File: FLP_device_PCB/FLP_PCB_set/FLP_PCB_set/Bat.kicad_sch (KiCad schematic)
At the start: 6 parts, among them J7 B2B-PH-K-S, U11 MCP73831-2-OT

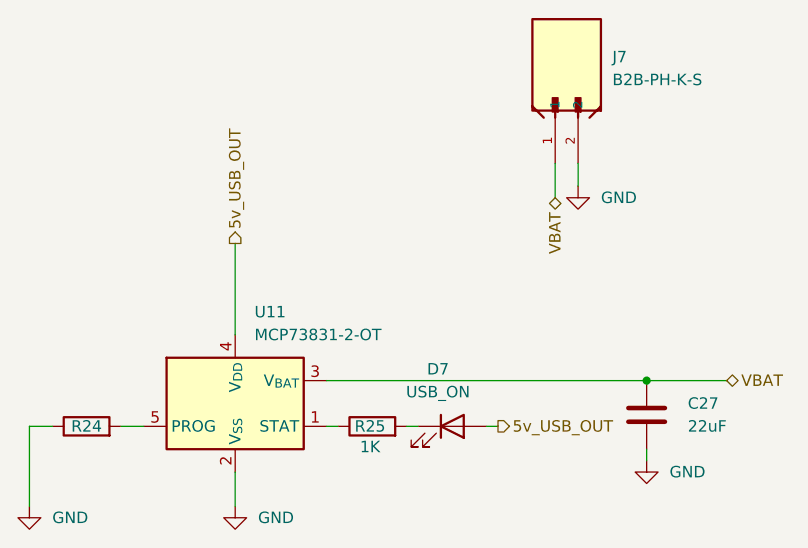
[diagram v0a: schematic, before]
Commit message: PCB fixing end adding description pdf
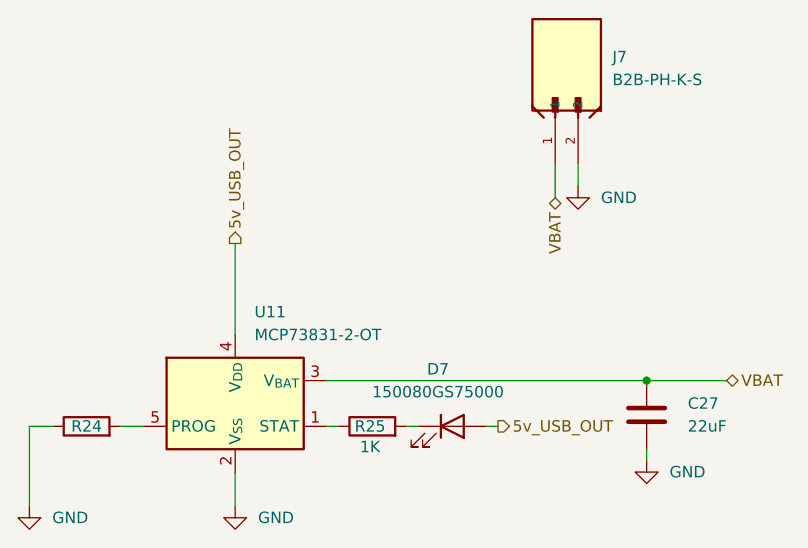
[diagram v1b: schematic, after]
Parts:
- D7: value USB_ON -> 150080GS75000
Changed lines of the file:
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@@
 			)
 		)
-		(property "Value" "USB_ON"
+		(property "Value" "150080GS75000"
 			(at 84.7725 63.5 0)
 			(effects

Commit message: PCB pdf add
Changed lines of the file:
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@@
 					(size 1.27 1.27)
 				)
-				(hide yes)
 			)
 		)
